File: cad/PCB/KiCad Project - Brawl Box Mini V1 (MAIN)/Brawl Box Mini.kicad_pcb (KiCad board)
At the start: 2 copper layers, 136 x 85 mm, 14 parts, among them J1 Conn_01x05_Socket, SW1 Power_Switch, SW2 SW_Push, SW3 SW_Push, SW4 SW_Push, SW5 SW_Push, SW6 SW_Push, SW7 SW_Push, U1 DEVKIT_V1_ESP32-WROOM-32, U2 MT3608_DC-DC_STEP_UP_CONVERTE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, U3 TP4056 Charging Module

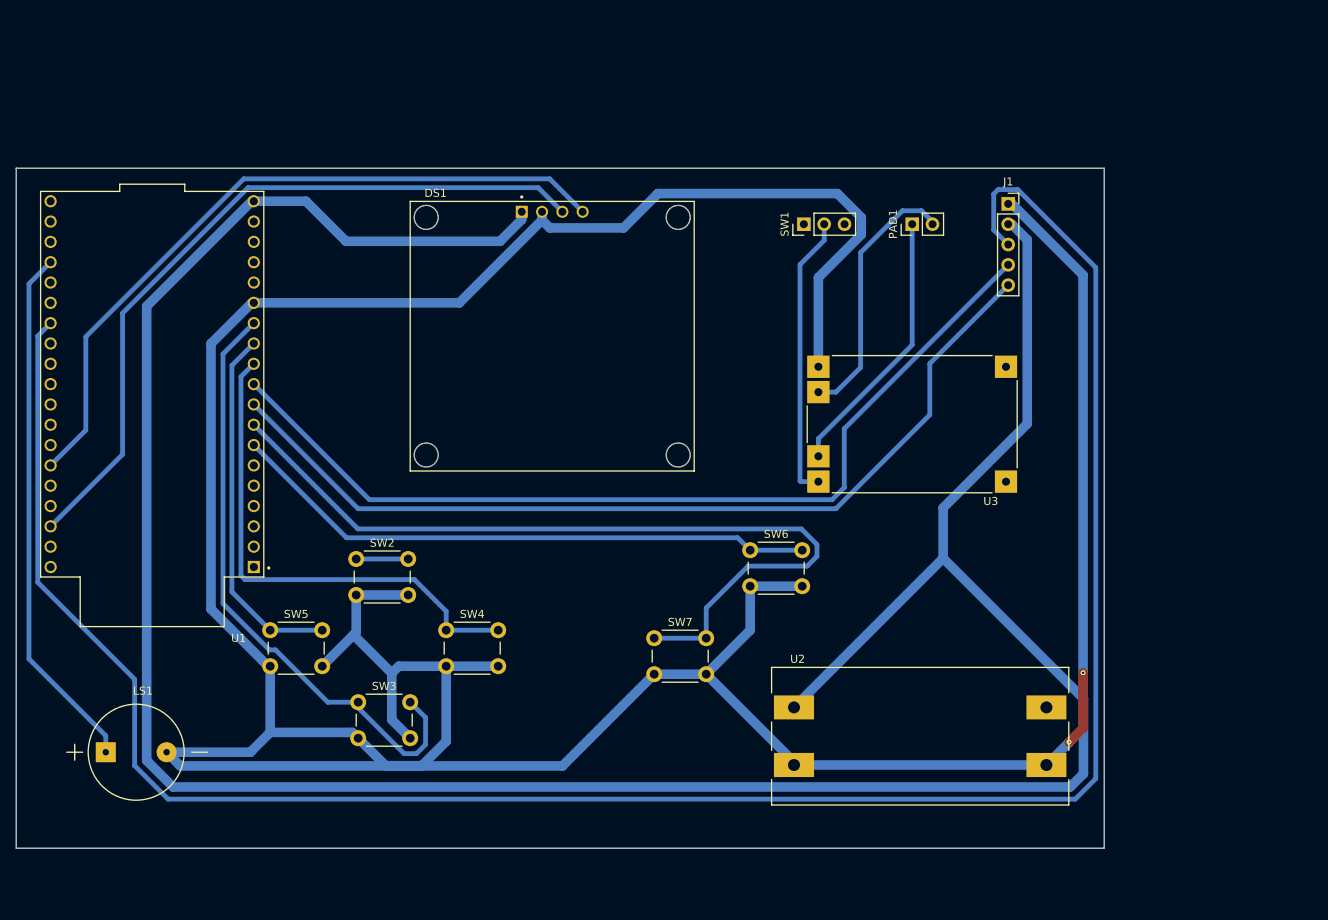
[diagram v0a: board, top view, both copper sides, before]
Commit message: Optimized Layout and Routing Single Layer
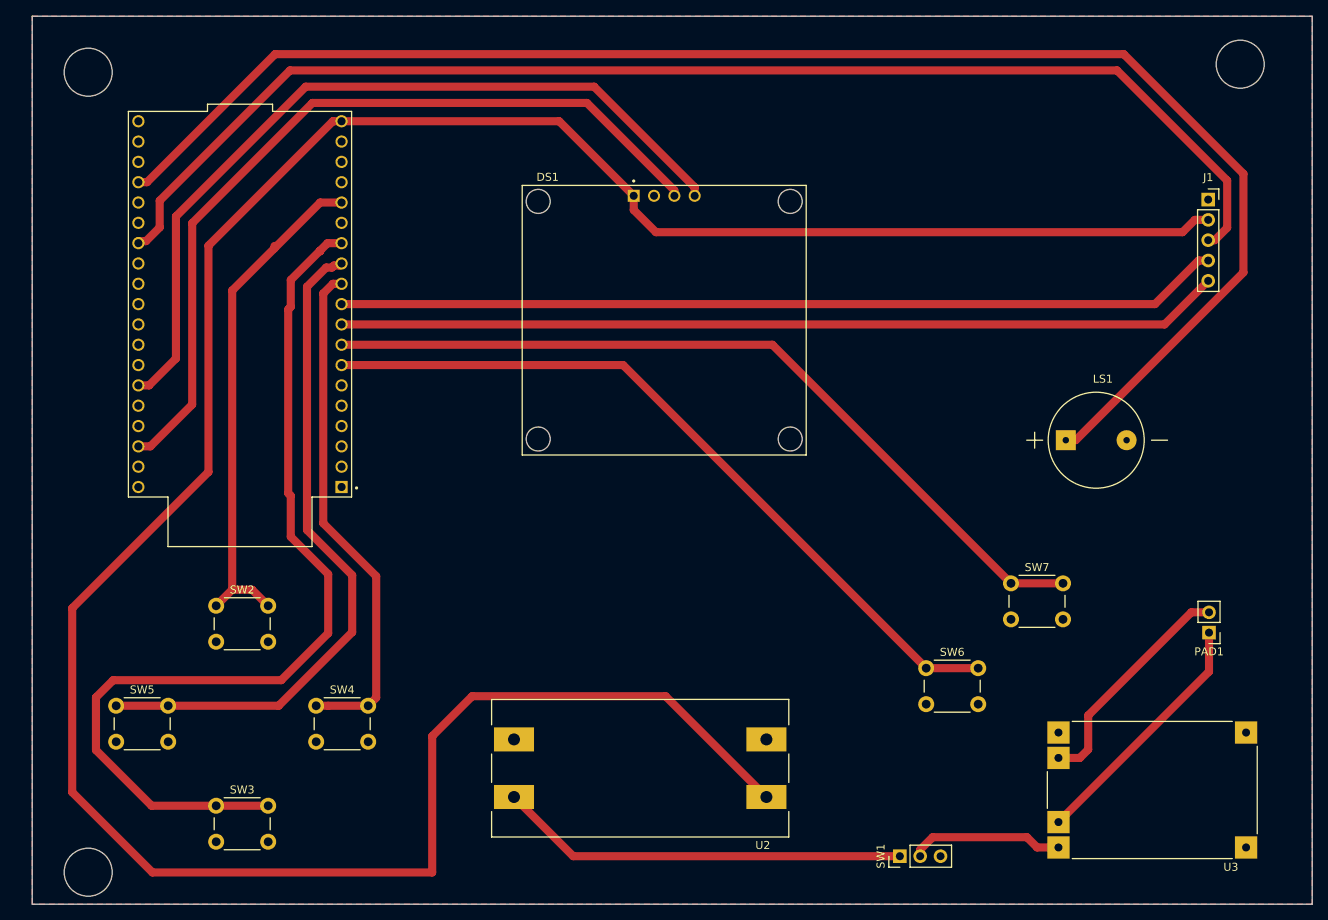
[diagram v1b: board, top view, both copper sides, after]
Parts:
- moved LS1 126.2 mm to (222.0, 83.0)
- moved SW1 79.9 mm to (197.5, 135.0)
- moved PAD1 63.1 mm to (236.1, 107.1), turned to 180 degrees
- moved U3 54.7 mm to (229.0, 126.7)
- moved SW7 45.1 mm to (211.3, 100.9)
- moved U2 35.2 mm to (165.0, 124.0), turned to 180 degrees
- moved SW6 26.5 mm to (200.8, 111.5)
- moved J1 25.0 mm to (236.0, 52.9)
- moved SW3 22.0 mm to (112.0, 128.7)
- moved SW5 21.4 mm to (99.5, 116.2)
- moved SW4 18.8 mm to (124.5, 116.2)
- moved SW2 18.5 mm to (112.0, 103.7)
- moved U1 14.8 mm to (115.0, 66.0)
- moved DS1 14.1 mm to (168.0, 68.0)
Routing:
- net GND: track 476.2 -> 0.00 mm, vias 2 -> 0
- net /BUZZER: track 66.3 -> 194.2 mm
- net /ENC_SW: track 271.9 -> 161.8 mm
- net /BTN_UP: track 6.50 -> 64.3 mm
- net Net-(SW1-A): track 0.00 -> 51.3 mm
- net /BTN_DOWN: track 76.7 -> 118.0 mm
- net /BTN_LEFT: track 45.5 -> 84.4 mm
- net /BTN_A: track 74.0 -> 95.3 mm
- net Net-(SW1-B): track 35.7 -> 19.3 mm
- net /OLED_SDA: track 89.9 -> 101.7 mm
- net +5V: track 340.4 -> 329.7 mm
- net /OLED_SCK: track 93.1 -> 103.3 mm
- net /ENC_DT: track 116.7 -> 110.6 mm
- net /ENC_CLK: track 115.0 -> 110.6 mm
- net Net-(PAD1-Pin_2): track 32.9 -> 28.9 mm
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- added copper zone on F.Cu, net GND
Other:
- board size 136 x 85 mm -> 160 x 111 mm

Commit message: Final PCB Layout
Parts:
- added G***: LOGO, LOGO, F.Cu at (155.4, 96.0)
- moved U3 4.99 mm to (234.0, 126.7)
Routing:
- net Net-(SW1-B): track 19.3 -> 25.6 mm
- net Net-(PAD1-Pin_2): track 28.9 -> 26.7 mm
- net /BAT_P: track 31.5 -> 29.4 mm
- net +5V: track 329.7 -> 330.8 mm
- net /BTN_UP: track 64.3 -> 65.2 mm
- net /OLED_SCK: track 103.3 -> 102.6 mm
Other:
- outline, holes or cut-outs redrawn
- board text added: "By Team Vega"
- board text added: "Des: Aarya Tanwade ;)"
